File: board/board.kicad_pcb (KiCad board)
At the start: 4 copper layers, 29 x 13 mm, 8 parts, among them J1 osf.011, J2 osf.011

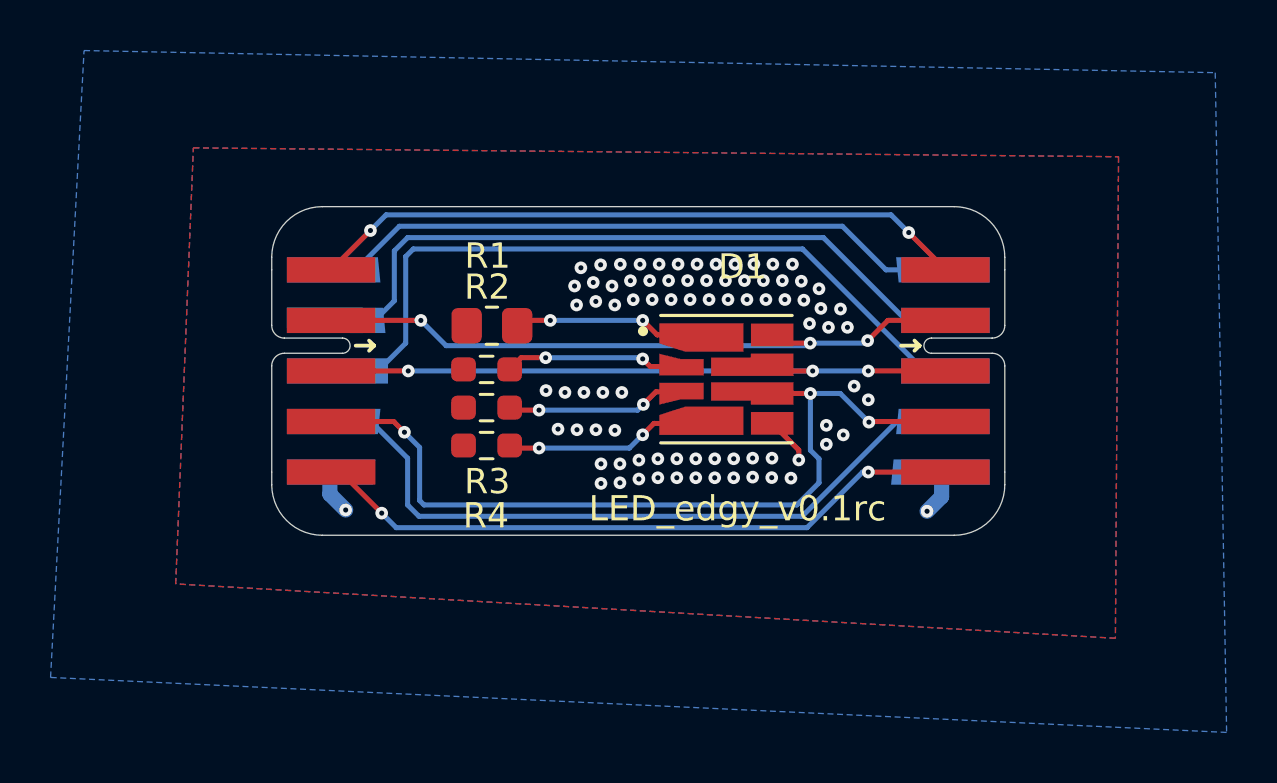
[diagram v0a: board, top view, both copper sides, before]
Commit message: Update Schmetaic Design for better heat management
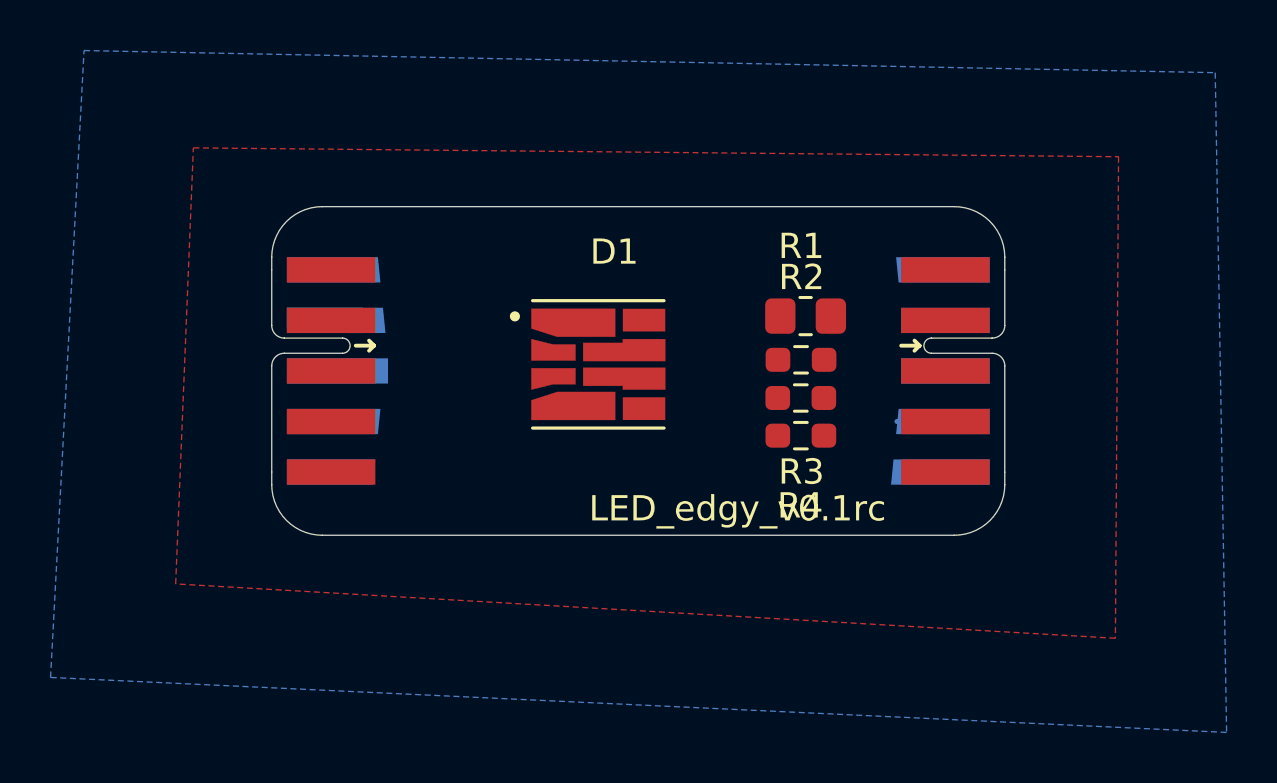
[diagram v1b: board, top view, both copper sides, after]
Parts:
- moved R2 12.4 mm to (160.9, 96.1)
- moved R4 12.4 mm to (160.9, 99.1)
- moved R3 12.4 mm to (160.9, 97.6)
- moved R1 12.4 mm to (161.1, 94.3)
- moved D1 5.10 mm to (152.9, 96.2)
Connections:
- D1 pad 1: Net-(D1-Pad1) -> Net-(J1-5V)
- D1 pad 2: Net-(D1-Pad2) -> Net-(J1-5V)
- D1 pad 3: Net-(D1-Pad3) -> Net-(J1-5V)
- D1 pad 4: Net-(D1-Pad4) -> Net-(J1-5V)
- J1 pad 10: Net-(J1-Pad10) -> Net-(J1-5V)
- J1 pad 2: Net-(D1-Pad8) -> Net-(J1-GPIO0)
- J1 pad 3: Net-(D1-Pad7) -> Net-(J1-GPIO1)
- J1 pad 4: Net-(D1-Pad6) -> Net-(J1-GPIO2)
- J1 pad 5: Net-(D1-Pad5) -> Net-(J1-GPIO3)
- J2 pad 10: Net-(J1-Pad10) -> Net-(J1-5V)
- J2 pad 2: Net-(D1-Pad8) -> Net-(J1-GPIO0)
- J2 pad 3: Net-(D1-Pad7) -> Net-(J1-GPIO1)
- J2 pad 4: Net-(D1-Pad6) -> Net-(J1-GPIO2)
- J2 pad 5: Net-(D1-Pad5) -> Net-(J1-GPIO3)
- R1 pad 1: Net-(J1-Pad10) -> Net-(D1-Pad8)
- R1 pad 2: Net-(D1-Pad1) -> Net-(J1-GPIO0)
- R2 pad 1: Net-(J1-Pad10) -> Net-(D1-Pad7)
- R2 pad 2: Net-(D1-Pad2) -> Net-(J1-GPIO1)
- R3 pad 1: Net-(J1-Pad10) -> Net-(D1-Pad6)
- R3 pad 2: Net-(D1-Pad3) -> Net-(J1-GPIO2)
- R4 pad 1: Net-(J1-Pad10) -> Net-(D1-Pad5)
- R4 pad 2: Net-(D1-Pad4) -> Net-(J1-GPIO3)
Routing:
- net Net-(D1-Pad6): track 33.3 -> 0.00 mm, vias 3 -> 0
- net Net-(D1-Pad5): track 31.0 -> 0.00 mm, vias 3 -> 0
- net Net-(J1-GND-Pad8): track 30.1 -> 0.83 mm
- net Net-(J1-GPIO5): track 28.4 -> 1.55 mm
- net Net-(D1-Pad8): track 26.8 -> 0.00 mm, vias 3 -> 0
- net Net-(J1-3.3V): track 28.4 -> 1.87 mm
- net Net-(J1-GND-Pad1): track 26.1 -> 0.03 mm, vias 2 -> 0
- net Net-(D1-Pad7): track 26.0 -> 0.00 mm, vias 3 -> 0
- net Net-(J1-GPIO4): track 25.6 -> 0.00 mm
- net Net-(D1-Pad4): track 7.21 -> 0.00 mm, vias 2 -> 0
- net Net-(D1-Pad2): track 7.13 -> 0.00 mm, vias 2 -> 0
- net Net-(D1-Pad3): track 7.11 -> 0.00 mm, vias 2 -> 0
- net Net-(D1-Pad1): track 6.79 -> 0.00 mm, vias 2 -> 0
- net Net-(J1-Pad10): track 3.55 -> 0.00 mm, vias 81 -> 0
- added copper zone on B.Cu, net Net-(J1-5V)
- added copper zone on F.Cu, net Net-(J1-5V)
- added copper zone on In1.Cu, net Net-(J1-5V)
- added copper zone on In2.Cu, net Net-(J1-5V)
- removed copper zone on B.Cu, net Net-(J1-Pad10)
- removed copper zone on F.Cu, net Net-(J1-Pad10)
- removed copper zone on In1.Cu, net Net-(J1-Pad10)
- removed copper zone on In2.Cu, net Net-(J1-Pad10)

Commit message: Save changes
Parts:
- moved D1 1.74 mm to (151.2, 96.3)
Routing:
- net Net-(J1-GND-Pad1): track 0.03 -> 53.1 mm, vias 0 -> 2
- net Net-(J1-GPIO3): track 0.38 -> 29.7 mm
- net Net-(J1-GPIO5): track 1.55 -> 30.0 mm
- net Net-(J1-GPIO4): track 0.00 -> 26.0 mm
- net Net-(D1-Pad8): track 0.00 -> 9.35 mm, vias 0 -> 2
- net Net-(D1-Pad5): track 0.00 -> 8.74 mm, vias 0 -> 2
- net Net-(D1-Pad7): track 0.00 -> 7.63 mm, vias 0 -> 2
- net Net-(J1-5V): track 0.00 -> 7.42 mm, vias 0 -> 2
- net Net-(D1-Pad6): track 0.00 -> 7.37 mm, vias 0 -> 2
- net Net-(J1-GPIO2): track 0.00 -> 5.19 mm
- net Net-(J1-GPIO1): track 0.00 -> 4.98 mm
- net Net-(J1-GPIO0): track 0.00 -> 4.60 mm
- net Net-(J1-GND-Pad8): track 0.83 -> 4.99 mm
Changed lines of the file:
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@@
   )
   (footprint "GW_J9LHS1:LED_GW_J9LHS1.4M-C1C7-2+58+MQ+30A-1-100-R33" (layer "F.Cu")
-    (at 152.92 96.24)
+    (at 151.18 96.3)
     (property "MANUFACTURER" "OSRAM Opto Semiconductors")
     (property "MAXIMUM_PACKAGE_HEIGHT" "1.2 mm")
@@
     (effects (font (size 1 1) (thickness 0.15)))
   )
-  (segment (start 166.65 92.475) (end 166.65 92.5) (width 0.2) (layer "F.Cu") (net 6))
+  (segment (start 149.37 95.8) (end 149.37 96.8) (width 0.6) (layer "F.Cu") (net 1))
+  (segment (start 149.37 96.8) (end 149.37 98.05) (width 0.6) (layer "F.Cu") (net 1))
+  (segment (start 149.37 95.8) (end 149.37 94.55) (width 0.6) (layer "F.Cu") (net 1))
+  (via (at 142.97 102.11) (size 0.5) (drill 0.2) (layers "F.Cu" "B.Cu") (net 1))
+  (via (at 165.49 102.11) (size 0.5) (drill 0.2) (layers "F.Cu" "B.Cu") (net 1))
+  (segment (start 142.3 101.44) (end 142.97 102.11) (width 0.6) (layer "B.Cu") (net 1))
+  (segment (start 166.5 101.1) (end 165.49 102.11) (width 0.6) (layer "B.Cu") (net 1))
+  (segment (start 142.3 100.5) (end 142.3 101.44) (width 0.6) (layer "B.Cu") (net 1))
+  (segment (start 166.5 100.5) (end 166.5 101.1) (width 0.6) (layer "B.Cu") (net 1))
+  (segment (start 159.9475 95.98) (end 160.0275 96.06) (width 0.2) (layer "F.Cu") (net 2))
+  (segment (start 152.99 95.735) (end 154.435 95.735) (width 0.2) (layer "F.Cu") (net 2))
+  (segment (start 158.88 95.98) (end 159.9475 95.98) (width 0.2) (layer "F.Cu") (net 2))
+  (segment (start 159.7025 95.735) (end 160.0275 96.06) (width 0.2) (layer "F.Cu") (net 2))
+  (segment (start 154.435 95.735) (end 154.5 95.8) (width 0.2) (layer "F.Cu") (net 2))
+  (via (at 154.5 95.8) (size 0.5) (drill 0.2) (layers "F.Cu" "B.Cu") (net 2))
+  (via (at 158.88 95.98) (size 0.5) (drill 0.2) (layers "F.Cu" "B.Cu") (net 2))
+  (segment (start 158.7 95.8) (end 158.88 95.98) (width 0.2) (layer "B.Cu") (net 2))
+  (segment (start 154.5 95.8) (end 158.7 95.8) (width 0.2) (layer "B.Cu") (net 2))
+  (segment (start 159.47 99.61) (end 160.02 99.06) (width 0.2) (layer "F.Cu") (net 3))
+  (segment (start 154.18 98.05) (end 154.51 98.38) (width 0.2) (layer "F.Cu") (net 3))
+  (segment (start 152.99 98.05) (end 154.18 98.05) (width 0.2) (layer "F.Cu") (net 3))
+  (segment (start 159.47 100.2) (end 159.47 99.61) (width 0.2) (layer "F.Cu") (net 3))
+  (via (at 159.47 100.2) (size 0.5) (drill 0.2) (layers "F.Cu" "B.Cu") (net 3))
+  (via (at 154.51 98.38) (size 0.5) (drill 0.2) (layers "F.Cu" "B.Cu") (net 3))
+  (segment (start 156.33 100.2) (end 159.47 100.2) (width 0.2) (layer "B.Cu") (net 3))
+  (segment (start 154.51 98.38) (end 156.33 100.2) (width 0.2) (layer "B.Cu") (net 3))
+  (segment (start 159.9575 97.63) (end 160.0175 97.57) (width 0.2) (layer "F.Cu") (net 4))
+  (segment (start 152.99 96.865) (end 154.335 96.865) (width 0.2) (layer "F.Cu") (net 4))
+  (segment (start 154.335 96.865) (end 154.51 97.04) (width 0.2) (layer "F.Cu") (net 4))
+  (segment (start 158.86 97.63) (end 159.9575 97.63) (width 0.2) (layer "F.Cu") (net 4))
+  (via (at 158.86 97.63) (size 0.5) (drill 0.2) (layers "F.Cu" "B.Cu") (net 4))
+  (via (at 154.51 97.04) (size 0.5) (drill 0.2) (layers "F.Cu" "B.Cu") (net 4))
+  (segment (start 158.27 97.04) (end 158.86 97.63) (width 0.2) (layer "B.Cu") (net 4))
+  (segment (start 154.51 97.04) (end 158.27 97.04) (width 0.2) (layer "B.Cu") (net 4))
+  (segment (start 152.99 94.55) (end 154.64 94.55) (width 0.2) (layer "F.Cu") (net 5))
+  (segment (start 154.64 94.55) (end 154.65 94.54) (width 0.2) (layer "F.Cu") (net 5))
+  (segment (start 159.87 94.08) (end 160.12 94.33) (width 0.2) (layer "F.Cu") (net 5))
+  (segment (start 159.9 94.55) (end 160.12 94.33) (width 0.2) (layer "F.Cu") (net 5))
+  (segment (start 159.87 92.94) (end 159.87 94.08) (width 0.2) (layer "F.Cu") (net 5))
+  (via (at 159.87 92.94) (size 0.5) (drill 0.2) (layers "F.Cu" "B.Cu") (net 5))
+  (via (at 154.65 94.54) (size 0.5) (drill 0.2) (layers "F.Cu" "B.Cu") (net 5))
+  (segment (start 158.27 94.54) (end 159.87 92.94) (width 0.2) (layer "B.Cu") (net 5))
+  (segment (start 154.65 94.54) (end 158.27 94.54) (width 0.2) (layer "B.Cu") (net 5))
+  (segment (start 143.4 91.06) (end 143.4 91.45) (width 0.2) (layer "F.Cu") (net 6))
+  (segment (start 166.65 92.5) (end 166.65 91.37) (width 0.2) (layer "F.Cu") (net 6))
+  (segment (start 142.35 92.5) (end 144.55 90.3) (width 0.2) (layer "F.Cu") (net 6))
+  (segment (start 164.45 90.3) (end 166.65 92.5) (width 0.2) (layer "F.Cu") (net 6))
+  (segment (start 144.55 90.3) (end 164.45 90.3) (width 0.2) (layer "F.Cu") (net 6))
+  (segment (start 166.65 91.37) (end 166.41 91.13) (width 0.2) (layer "F.Cu") (net 6))
+  (segment (start 143.4 91.45) (end 142.35 92.5) (width 0.2) (layer "F.Cu") (net 6))
+  (via (at 143.4 91.06) (size 0.5) (drill 0.2) (layers "F.Cu" "B.Cu") (net 6))
+  (via (at 166.41 91.13) (size 0.5) (drill 0.2) (layers "F.Cu" "B.Cu") (net 6))
+  (segment (start 144.16 90.3) (end 143.4 91.06) (width 0.2) (layer "B.Cu") (net 6))
+  (segment (start 144.94 90.3) (end 144.16 90.3) (width 0.2) (layer "B.Cu") (net 6))
+  (segment (start 165.58 90.3) (end 144.94 90.3) (width 0.2) (layer "B.Cu") (net 6))
+  (segment (start 166.41 91.13) (end 165.58 90.3) (width 0.2) (layer "B.Cu") (net 6))
+  (segment (start 162.12 94.33) (end 162.29 94.5) (width 0.2) (layer "F.Cu") (net 7))
+  (segment (start 162.29 94.5) (end 166.65 94.5) (width 0.2) (layer "F.Cu") (net 7))
+  (segment (start 162.2925 96.5) (end 166.65 96.5) (width 0.2) (layer "F.Cu") (net 8))
+  (segment (start 161.8525 96.06) (end 162.2925 96.5) (width 0.2) (layer "F.Cu") (net 8))
+  (segment (start 161.8425 97.57) (end 162.7725 98.5) (width 0.2) (layer "F.Cu") (net 9))
+  (segment (start 162.7725 98.5) (end 166.65 98.5) (width 0.2) (layer "F.Cu") (net 9))
   (segment (start 142.725 100.5) (end 142.35 100.5) (width 0.2) (layer "F.Cu") (net 10))
+  (segment (start 163.285 102.005) (end 163.285 100.5) (width 0.2) (layer "F.Cu") (net 10))
+  (segment (start 161.845 99.06) (end 163.285 100.5) (width 0.2) (layer "F.Cu") (net 10))
+  (segment (start 143.82 101.97) (end 143.82 102.5) (width 0.2) (layer "F.Cu") (net 10))
+  (segment (start 143.82 102.5) (end 144.02 102.7) (width 0.2) (layer "F.Cu") (net 10))
+  (segment (start 142.35 100.5) (end 143.82 101.97) (width 0.2) (layer "F.Cu") (net 10))
+  (segment (start 162.59 102.7) (end 163.285 102.005) (width 0.2) (layer "F.Cu") (net 10))
+  (segment (start 163.285 100.5) (end 166.65 100.5) (width 0.2) (layer "F.Cu") (net 10))
+  (segment (start 144.02 102.7) (end 162.59 102.7) (width 0.2) (layer "F.Cu") (net 10))
+  (segment (start 165.22 90.64) (end 144.96 90.64) (width 0.2) (layer "B.Cu") (net 11))
+  (segment (start 144.96 90.64) (end 144.947 90.627) (width 0.2) (layer "B.Cu") (net 11))
+  (segment (start 144.48 90.65458) (end 142.63458 92.5) (width 0.2) (layer "B.Cu") (net 11))
+  (segment (start 166.6 92.5) (end 166.6 92.02) (width 0.2) (layer "B.Cu") (net 11))
+  (segment (start 166.6 92.02) (end 165.22 90.64) (width 0.2) (layer "B.Cu") (net 11))
+  (segment (start 144.48 90.627) (end 144.48 90.65458) (width 0.2) (layer "B.Cu") (net 11))
+  (segment (start 142.63458 92.5) (end 142.4 92.5) (width 0.2) (layer "B.Cu") (net 11))
+  (segment (start 144.947 90.627) (end 144.48 90.627) (width 0.2) (layer "B.Cu") (net 11))
+  (segment (start 162.27 90.967) (end 165.803 94.5) (width 0.2) (layer "B.Cu") (net 12))
   (segment (start 166.65 94.5) (end 165.1 94.5) (width 0.2) (layer "B.Cu") (net 12))
+  (segment (start 145.783 90.967) (end 162.27 90.967) (width 0.2) (layer "B.Cu") (net 12))
+  (segment (start 145.1 93.26) (end 145.1 91.65) (width 0.2) (layer "B.Cu") (net 12))
+  (segment (start 143.86 94.5) (end 145.1 93.26) (width 0.2) (layer "B.Cu") (net 12))
+  (segment (start 142.1 94.5) (end 143.86 94.5) (width 0.2) (layer "B.Cu") (net 12))
+  (segment (start 165.803 94.5) (end 166.65 94.5) (width 0.2) (layer "B.Cu") (net 12))
+  (segment (start 145.1 91.65) (end 145.783 90.967) (width 0.2) (layer "B.Cu") (net 12))
   (segment (start 166.65 96.5) (end 165.825 96.5) (width 0.2) (layer "B.Cu") (net 13))
+  (segment (start 166.65 96.5) (end 165.81 96.5) (width 0.2) (layer "B.Cu") (net 13))
+  (segment (start 165.81 96.5) (end 163.46 94.15) (width 0.2) (layer "B.Cu") (net 13))
   (segment (start 166.6 98.5) (end 164.732948 98.5) (width 0.2) (layer "B.Cu") (net 14))
   (zone (net 1) (net_name "Net-(J1-5V)") (layer "F.Cu") (hatch edge 0.508)

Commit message: Update PCB Design | Add routes
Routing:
- net Net-(J1-GPIO1): track 4.98 -> 34.2 mm, vias 0 -> 2
- net Net-(J1-3.3V): track 1.87 -> 29.2 mm
- net Net-(J1-GND-Pad8): track 4.99 -> 31.6 mm
- net Net-(J1-GPIO2): track 5.19 -> 31.6 mm, vias 0 -> 2
- net Net-(J1-GPIO0): track 4.60 -> 28.5 mm, vias 0 -> 2
- net Net-(J1-5V): track 7.42 -> 16.7 mm, vias 2 -> 81
- net Net-(J1-GPIO5): track 30.0 -> 28.8 mm
